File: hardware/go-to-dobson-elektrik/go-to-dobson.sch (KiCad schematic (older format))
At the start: 1 part

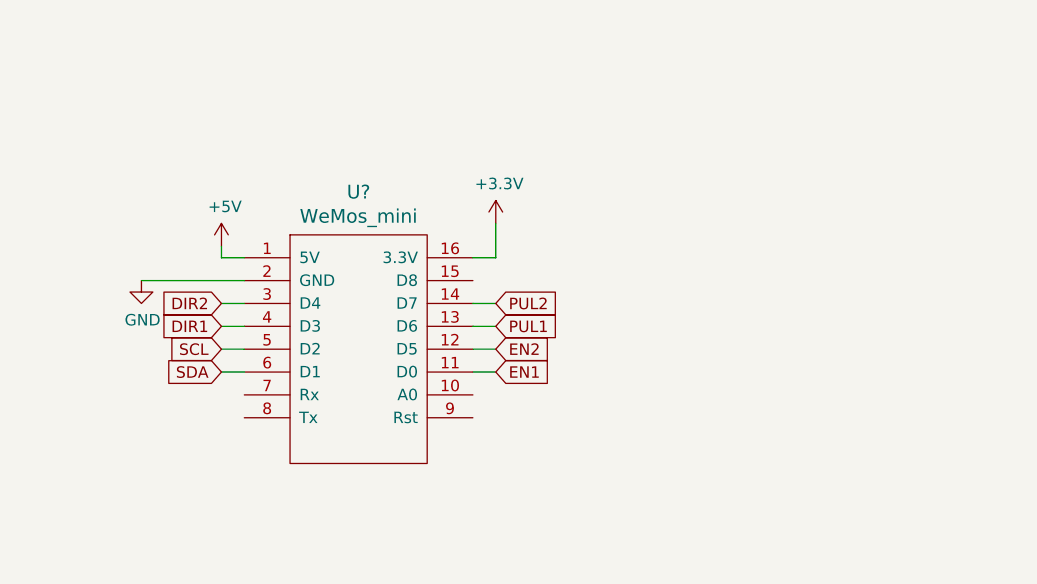
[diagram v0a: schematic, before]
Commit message: schrittmotoren in eigene Klasse ausgelagert kommunikation stellaris-> controller funktioniert
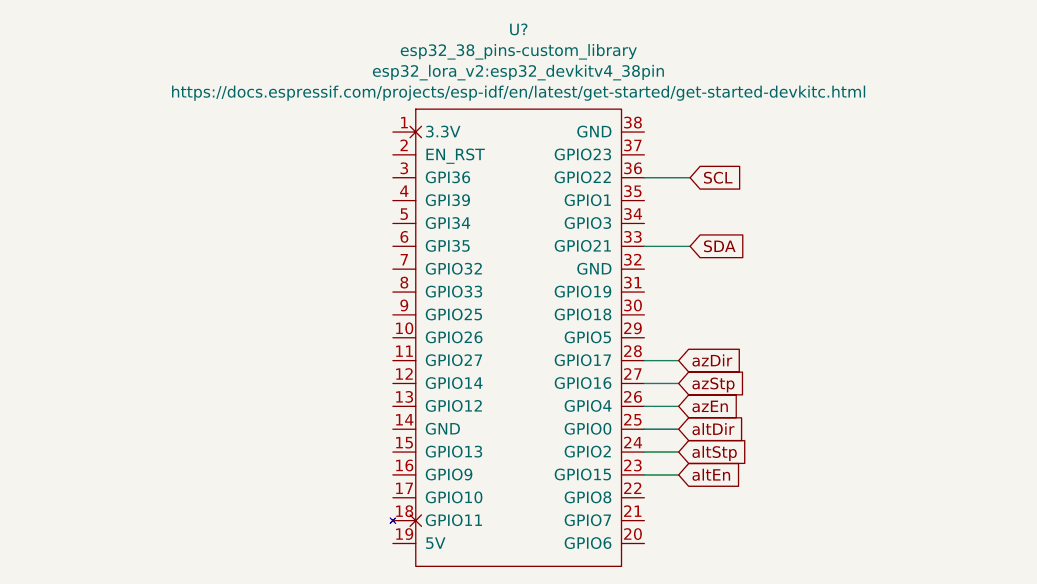
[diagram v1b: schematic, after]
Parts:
- removed U?: WeMos_mini, symbol wemos_mini:WeMos_mini
- added U?: esp32_38_pins-custom_library, esp32_lora_v2:esp32_devkitv4_38pin, symbol mighty_esp32_38_pins-custom_library:esp32_38_pins-custom_library
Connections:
- net SCL: now also U?.36 (GPIO22)
- net SDA: now also U?.33 (GPIO21)
- new net altDir: U?.25 (GPIO0)
- new net altEn: U?.23 (GPIO15)
- new net altStp: U?.24 (GPIO2)
- new net azDir: U?.28 (GPIO17)
- new net azEn: U?.26 (GPIO4)
- new net azStp: U?.27 (GPIO16)
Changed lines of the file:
@@
 $EndDescr
 $Comp
-L wemos_mini:WeMos_mini U?
-U 1 1 6022B98D
-P 5400 2650
-F 0 "U?" H 5400 3287 60  0000 C CNN
-F 1 "WeMos_mini" H 5400 3181 60  0000 C CNN
-F 2 "" H 5950 1950 60  0000 C CNN
-F 3 "http://www.wemos.cc/Products/d1_mini.html" H 5950 1950 60  0001 C CNN
-	1    5400 2650
+L mighty_esp32_38_pins-custom_library:esp32_38_pins-custom_library U?
+U 1 1 603819DF
+P 5750 1950
+F 0 "U?" H 6100 2597 50  0000 C CNN
+F 1 "esp32_38_pins-custom_library" H 6100 2506 50  0000 C CNN
+F 2 "esp32_lora_v2:esp32_devkitv4_38pin" H 6100 2415 50  0000 C CNN
+F 3 "https://docs.espressif.com/projects/esp-idf/en/latest/get-started/get-started-devkitc.html" H 6100 2324 50  0000 C CNN
+	1    5750 1950
 	1    0    0    -1
 $EndComp
-$Comp
-L power:+5V #PWR?
-U 1 1 6022C354
-P 4800 2250
-F 0 "#PWR?" H 4800 2100 50  0001 C CNN
-F 1 "+5V" H 4815 2423 50  0000 C CNN
-F 2 "" H 4800 2250 50  0001 C CNN
-F 3 "" H 4800 2250 50  0001 C CNN
-	1    4800 2250
-	1    0    0    -1
-$EndComp
-$Comp
-L power:GND #PWR?
-U 1 1 6022CC0A
-P 4450 2400
-F 0 "#PWR?" H 4450 2150 50  0001 C CNN
-F 1 "GND" H 4455 2227 50  0000 C CNN
-F 2 "" H 4450 2400 50  0001 C CNN
-F 3 "" H 4450 2400 50  0001 C CNN
-	1    4450 2400
-	1    0    0    -1
-$EndComp
-$Comp
-L power:+3.3V #PWR?
-U 1 1 6022D3E5
-P 6000 2150
-F 0 "#PWR?" H 6000 2000 50  0001 C CNN
-F 1 "+3.3V" H 6015 2323 50  0000 C CNN
-F 2 "" H 6000 2150 50  0001 C CNN
-F 3 "" H 6000 2150 50  0001 C CNN
-	1    6000 2150
-	1    0    0    -1
-$EndComp
-Text GLabel 4800 2800 0    50   Input ~ 0
+Text GLabel 6800 2750 2    50   Input ~ 0
+azDir
+Text GLabel 6800 2850 2    50   Input ~ 0
+azStp
+Text GLabel 6800 2950 2    50   Input ~ 0
+azEn
+Text GLabel 6800 3050 2    50   Input ~ 0
+altDir
+Text GLabel 6800 3150 2    50   Input ~ 0
+altStp
+Text GLabel 6800 3250 2    50   Input ~ 0
+altEn
+Text GLabel 6850 2250 2    50   Input ~ 0
 SDA
-Text GLabel 4800 2700 0    50   Input ~ 0
+Text GLabel 6850 1950 2    50   Input ~ 0
 SCL
-Text GLabel 4800 2600 0    50   Input ~ 0
-DIR1
-Text GLabel 4800 2500 0    50   Input ~ 0
-DIR2
-Text GLabel 6000 2800 2    50   Input ~ 0
-EN1
-Text GLabel 6000 2700 2    50   Input ~ 0
-EN2
-Text GLabel 6000 2600 2    50   Input ~ 0
-PUL1
-Text GLabel 6000 2500 2    50   Input ~ 0
-PUL2
 Wire Wire Line
-	4900 2800 4800 2800
+	6650 1950 6850 1950
 Wire Wire Line
-	4900 2700 4800 2700
+	6850 2250 6650 2250
 Wire Wire Line
-	4900 2600 4800 2600
+	6650 2750 6800 2750
 Wire Wire Line
-	4900 2500 4800 2500
+	6650 2850 6800 2850
 Wire Wire Line
-	4900 2400 4450 2400
+	6650 2950 6800 2950
 Wire Wire Line
-	4900 2300 4800 2300
+	6650 3050 6800 3050
 Wire Wire Line
-	4800 2300 4800 2250
+	6650 3150 6800 3150
 Wire Wire Line
-	5900 2500 6000 2500
-Wire Wire Line
-	5900 2600 6000 2600
-Wire Wire Line
-	5900 2700 6000 2700
-Wire Wire Line
-	5900 2800 6000 2800
-Wire Wire Line
-	5900 2300 6000 2300
-Wire Wire Line
-	6000 2300 6000 2150
+	6650 3250 6800 3250
 $EndSCHEMATC
